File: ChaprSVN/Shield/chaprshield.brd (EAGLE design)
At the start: 100 x 80 mm, 2 parts

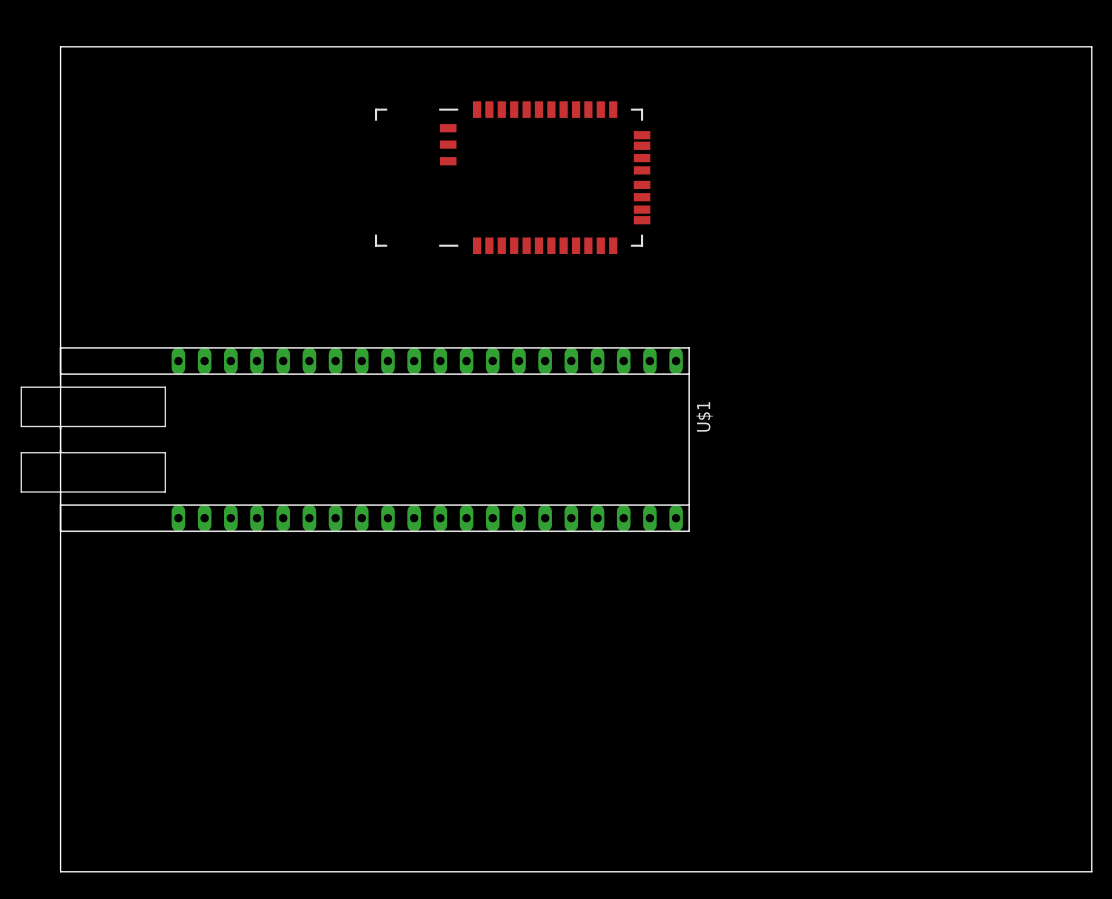
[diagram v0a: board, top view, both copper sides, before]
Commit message: Added pin headers and started wiring.
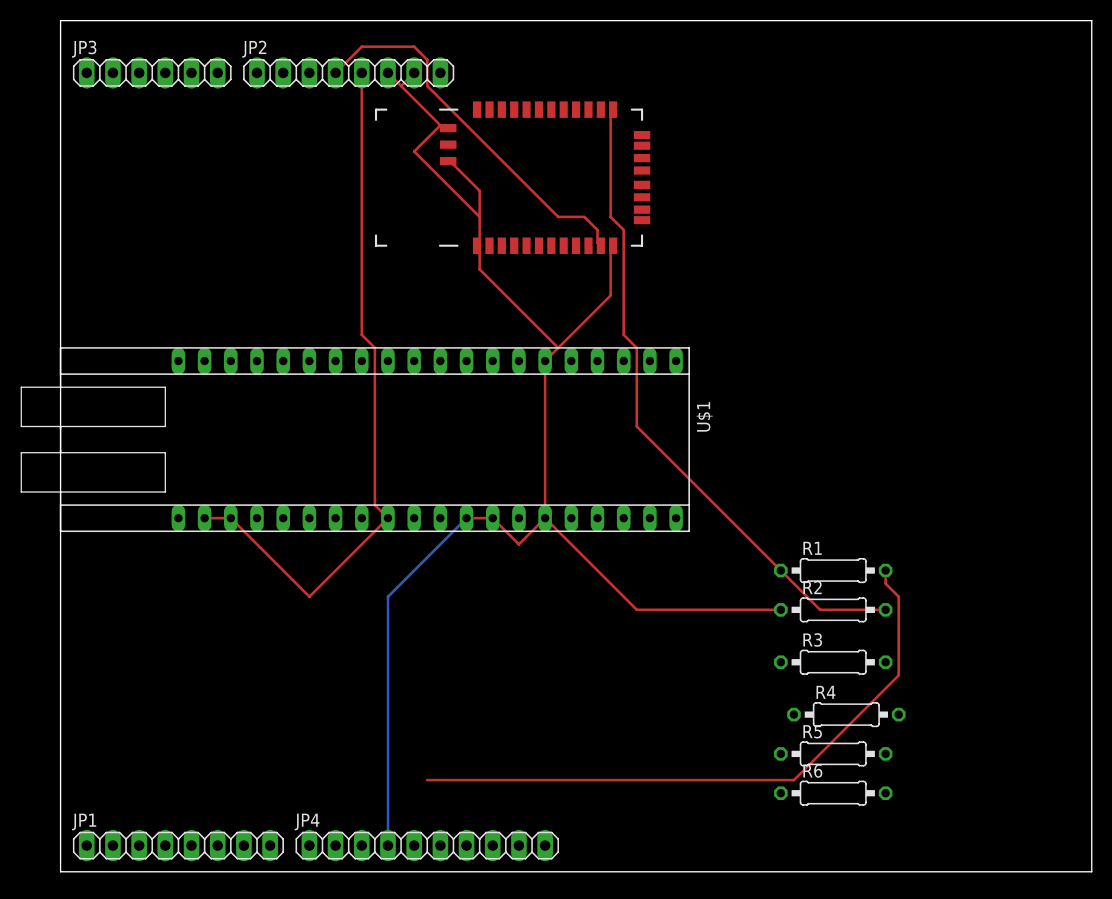
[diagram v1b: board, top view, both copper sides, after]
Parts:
- added JP1, JP2: (no value), pinhead:1X08
- added JP3: (no value), pinhead:1X06
- added JP4: (no value), pinhead:1X10
- added R1: 10k, resistor:0207/10
- added R2: 20k, resistor:0207/10
- added R3, R4, R5, R6: (no value), resistor:0207/10
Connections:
- removed net 5.0V(1): U$1.2
- removed net 5.0V(2): U$1.3
- removed net 5.0V(3): U$1.9
- new net N$1: JP2.5, U$1.2, U$1.3, U$1.9
- new net N$2: JP2.4, U$2.11
- new net N$3: JP4.5, R1.2
- new net N$4: R1.1, R2.2, U$2.13
- new net N$5: JP4.6, U$2.14
- net GND: now also JP2.6, JP2.7, JP4.4, R2.1
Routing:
- net GND: track 0.00 -> 146.1 mm
- net N$1: track 0.00 -> 68.3 mm
- net N$4: track 0.00 -> 63.4 mm
- net N$3: track 0.00 -> 60.6 mm
- net N$2: track 0.00 -> 37.0 mm
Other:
- board size 100 x 80 mm -> 100 x 82.5 mm
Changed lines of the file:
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@@
 <plain>
 <wire x1="0" y1="0" x2="100" y2="0" width="0" layer="20"/>
-<wire x1="100" y1="0" x2="100" y2="80" width="0" layer="20"/>
-<wire x1="100" y1="80" x2="0" y2="80" width="0" layer="20"/>
-<wire x1="0" y1="80" x2="0" y2="0" width="0" layer="20"/>
+<wire x1="100" y1="0" x2="100" y2="82.54" width="0" layer="20"/>
+<wire x1="100" y1="82.54" x2="0" y2="82.54" width="0" layer="20"/>
+<wire x1="0" y1="82.54" x2="0" y2="0" width="0" layer="20"/>
 </plain>
 <attributes>
@@
 <param name="RoutingGrid" value="50mil"/>
 <param name="tpViaShape" value="round"/>
-<param name="PrefDir.1" value="|"/>
+<param name="PrefDir.1" value="\"/>
 <param name="PrefDir.2" value="0"/>
 <param name="PrefDir.3" value="0"/>
@@
 <param name="PrefDir.14" value="0"/>
 <param name="PrefDir.15" value="0"/>
-<param name="PrefDir.16" value="-"/>
+<param name="PrefDir.16" value="*"/>
 <param name="cfVia" value="8"/>
 <param name="cfNonPref" value="5"/>
@@
 <element name="U$1" library="ChapR-Custom" package="VDIP2" value="VDIP2" x="35.56" y="41.91"/>
 <element name="U$2" library="SparkFun-RF" package="RN41" value="BLUETOOTH-RN41&quot;" x="46.99" y="67.31"/>
+<element name="JP1" library="pinhead" package="1X08" value="" x="11.43" y="2.54"/>
+<element name="JP2" library="pinhead" package="1X08" value="" x="27.94" y="77.47"/>
+<element name="JP3" library="pinhead" package="1X06" value="" x="8.89" y="77.47"/>
+<element name="JP4" library="pinhead" package="1X10" value="" x="35.56" y="2.54"/>
+<element name="R1" library="resistor" package="0207/10" value="10k" x="74.93" y="29.21"/>
+<element name="R2" library="resistor" package="0207/10" value="20k" x="74.93" y="25.4"/>
+<element name="R3" library="resistor" package="0207/10" value="" x="74.93" y="20.32"/>
+<element name="R4" library="resistor" package="0207/10" value="" x="76.2" y="15.24"/>
+<element name="R5" library="resistor" package="0207/10" value="" x="74.93" y="11.43"/>
+<element name="R6" library="resistor" package="0207/10" value="" x="74.93" y="7.62"/>
 </elements>
 <signals>
 <signal name="3.3V(2)">
 <contactref element="U$1" pad="38"/>
-</signal>
-<signal name="5.0V(1)">
-<contactref element="U$1" pad="2"/>
-</signal>
-<signal name="5.0V(2)">
-<contactref element="U$1" pad="3"/>
-</signal>
-<signal name="5.0V(3)">
-<contactref element="U$1" pad="9"/>
 </signal>
 <signal name="NC(1)">
@@
 <contactref element="U$2" pad="28"/>
 <contactref element="U$2" pad="29"/>
+<contactref element="JP4" pad="4"/>
+<contactref element="JP2" pad="6"/>
+<contactref element="JP2" pad="7"/>
+<contactref element="R2" pad="1"/>
+<wire x1="31.75" y1="77.47" x2="33.02" y2="76.2" width="0.254" layer="1"/>
+<wire x1="33.02" y1="76.2" x2="36.83" y2="72.39" width="0.254" layer="1"/>
+<wire x1="33.02" y1="76.2" x2="34.29" y2="77.47" width="0.254" layer="1"/>
+<wire x1="40.64" y1="66.04" x2="40.64" y2="63.5" width="0.254" layer="1"/>
+<wire x1="40.64" y1="63.5" x2="40.64" y2="60.96" width="0.254" layer="1"/>
+<wire x1="38.1" y1="68.58" x2="40.64" y2="66.04" width="0.254" layer="1"/>
+<wire x1="38.1" y1="68.58" x2="37.59" y2="68.91" width="0.254" layer="1"/>
+<wire x1="53.34" y1="55.88" x2="53.34" y2="60.96" width="0.254" layer="1"/>
+<wire x1="46.99" y1="49.53" x2="48.26" y2="50.8" width="0.254" layer="1"/>
+<wire x1="48.26" y1="50.8" x2="53.34" y2="55.88" width="0.254" layer="1"/>
+<wire x1="53.34" y1="60.96" x2="53.59" y2="60.71" width="0.254" layer="1"/>
+<wire x1="40.64" y1="58.42" x2="40.64" y2="60.96" width="0.254" layer="1"/>
+<wire x1="48.26" y1="50.8" x2="40.64" y2="58.42" width="0.254" layer="1"/>
+<wire x1="40.64" y1="60.96" x2="40.39" y2="60.71" width="0.254" layer="1"/>
+<wire x1="34.29" y1="69.85" x2="36.83" y2="72.39" width="0.254" layer="1"/>
+<wire x1="40.64" y1="63.5" x2="34.29" y2="69.85" width="0.254" layer="1"/>
+<wire x1="36.83" y1="72.39" x2="37.59" y2="72.11" width="0.254" layer="1"/>
+<wire x1="41.91" y1="34.29" x2="39.37" y2="34.29" width="0.254" layer="1"/>
+<wire x1="44.45" y1="31.75" x2="46.99" y2="34.29" width="0.254" layer="1"/>
+<wire x1="41.91" y1="34.29" x2="44.45" y2="31.75" width="0.254" layer="1"/>
+<wire x1="55.88" y1="25.4" x2="69.85" y2="25.4" width="0.254" layer="1"/>
+<wire x1="46.99" y1="34.29" x2="55.88" y2="25.4" width="0.254" layer="1"/>
+<wire x1="31.75" y1="26.67" x2="31.75" y2="2.54" width="0.254" layer="16"/>
+<wire x1="39.37" y1="34.29" x2="31.75" y2="26.67" width="0.254" layer="16"/>
+<wire x1="46.99" y1="34.29" x2="46.99" y2="49.53" width="0.254" layer="1"/>
 <wire x1="56.39" y1="64.21" x2="56.39" y2="70.41" width="0" layer="19" extent="1-1"/>
-<wire x1="53.59" y1="60.71" x2="56.39" y2="64.21" width="0" layer="19" extent="1-1"/>
-<wire x1="46.99" y1="49.53" x2="53.59" y2="60.71" width="0" layer="19" extent="1-1"/>
-<wire x1="40.39" y1="60.71" x2="46.99" y2="49.53" width="0" layer="19" extent="1-1"/>
-<wire x1="37.59" y1="68.91" x2="40.39" y2="60.71" width="0" layer="19" extent="1-1"/>
-<wire x1="37.59" y1="72.11" x2="37.59" y2="68.91" width="0" layer="19" extent="1-1"/>
-<wire x1="46.99" y1="34.29" x2="46.99" y2="49.53" width="0" layer="19" extent="1-1"/>
-<wire x1="41.91" y1="34.29" x2="46.99" y2="34.29" width="0" layer="19" extent="1-1"/>
-<wire x1="39.37" y1="34.29" x2="41.91" y2="34.29" width="0" layer="19" extent="1-1"/>
+<wire x1="53.34" y1="60.96" x2="56.39" y2="64.21" width="0" layer="19" extent="1-1"/>
+</signal>
+<signal name="N$1">
+<contactref element="JP2" pad="5"/>
+<contactref element="U$1" pad="9"/>
+<contactref element="U$1" pad="3"/>
+<contactref element="U$1" pad="2"/>
+<wire x1="16.51" y1="34.29" x2="13.97" y2="34.29" width="0.254" layer="1"/>
+<wire x1="24.13" y1="26.67" x2="31.75" y2="34.29" width="0.254" layer="1"/>
+<wire x1="16.51" y1="34.29" x2="24.13" y2="26.67" width="0.254" layer="1"/>
+<wire x1="29.21" y1="52.07" x2="29.21" y2="77.47" width="0.254" layer="1"/>
+<wire x1="30.48" y1="50.8" x2="29.21" y2="52.07" width="0.254" layer="1"/>
+<wire x1="30.48" y1="35.56" x2="30.48" y2="50.8" width="0.254" layer="1"/>
+<wire x1="31.75" y1="34.29" x2="30.48" y2="35.56" width="0.254" layer="1"/>
+</signal>
+<signal name="N$2">
+<contactref element="JP2" pad="4"/>
+<contactref element="U$2" pad="11"/>
+<wire x1="52.07" y1="62.23" x2="52.07" y2="60.96" width="0.254" layer="1"/>
+<wire x1="50.8" y1="63.5" x2="52.07" y2="62.23" width="0.254" layer="1"/>
+<wire x1="48.26" y1="63.5" x2="50.8" y2="63.5" width="0.254" layer="1"/>
+<wire x1="35.56" y1="76.2" x2="48.26" y2="63.5" width="0.254" layer="1"/>
+<wire x1="35.56" y1="78.74" x2="35.56" y2="76.2" width="0.254" layer="1"/>
+<wire x1="34.29" y1="80.01" x2="35.56" y2="78.74" width="0.254" layer="1"/>
+<wire x1="29.21" y1="80.01" x2="34.29" y2="80.01" width="0.254" layer="1"/>
+<wire x1="26.67" y1="77.47" x2="29.21" y2="80.01" width="0.254" layer="1"/>
+<wire x1="52.07" y1="60.96" x2="52.39" y2="60.71" width="0.254" layer="1"/>
+</signal>
+<signal name="N$3">
+<contactref element="R1" pad="2"/>
+<wire x1="80.01" y1="27.94" x2="80.01" y2="29.21" width="0.254" layer="1"/>
+<wire x1="81.28" y1="26.67" x2="80.01" y2="27.94" width="0.254" layer="1"/>
+<wire x1="81.28" y1="19.05" x2="81.28" y2="26.67" width="0.254" layer="1"/>
+<wire x1="71.12" y1="8.89" x2="81.28" y2="19.05" width="0.254" layer="1"/>
+<wire x1="35.56" y1="8.89" x2="71.12" y2="8.89" width="0.254" layer="1"/>
+<contactref element="JP4" pad="5"/>
+<wire x1="34.29" y1="2.54" x2="35.56" y2="8.89" width="0" layer="19" extent="1-1"/>
+</signal>
+<signal name="N$4">
+<contactref element="R1" pad="1"/>
+<contactref element="R2" pad="2"/>
+<contactref element="U$2" pad="13"/>
+<wire x1="53.34" y1="63.5" x2="53.34" y2="73.66" width="0.254" layer="1"/>
+<wire x1="54.61" y1="62.23" x2="53.34" y2="63.5" width="0.254" layer="1"/>
+<wire x1="54.61" y1="52.07" x2="54.61" y2="62.23" width="0.254" layer="1"/>
+<wire x1="55.88" y1="50.8" x2="54.61" y2="52.07" width="0.254" layer="1"/>
+<wire x1="55.88" y1="43.18" x2="55.88" y2="50.8" width="0.254" layer="1"/>
+<wire x1="69.85" y1="29.21" x2="55.88" y2="43.18" width="0.254" layer="1"/>
+<wire x1="53.34" y1="73.66" x2="53.59" y2="73.91" width="0.254" layer="1"/>
+<wire x1="73.66" y1="25.4" x2="80.01" y2="25.4" width="0.254" layer="1"/>
+<wire x1="69.85" y1="29.21" x2="73.66" y2="25.4" width="0.254" layer="1"/>
+</signal>
+<signal name="N$5">
+<contactref element="U$2" pad="14"/>
+<contactref element="JP4" pad="6"/>
+<wire x1="36.83" y1="2.54" x2="52.39" y2="73.91" width="0" layer="19" extent="1-1"/>
 </signal>
 </signals>

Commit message: 
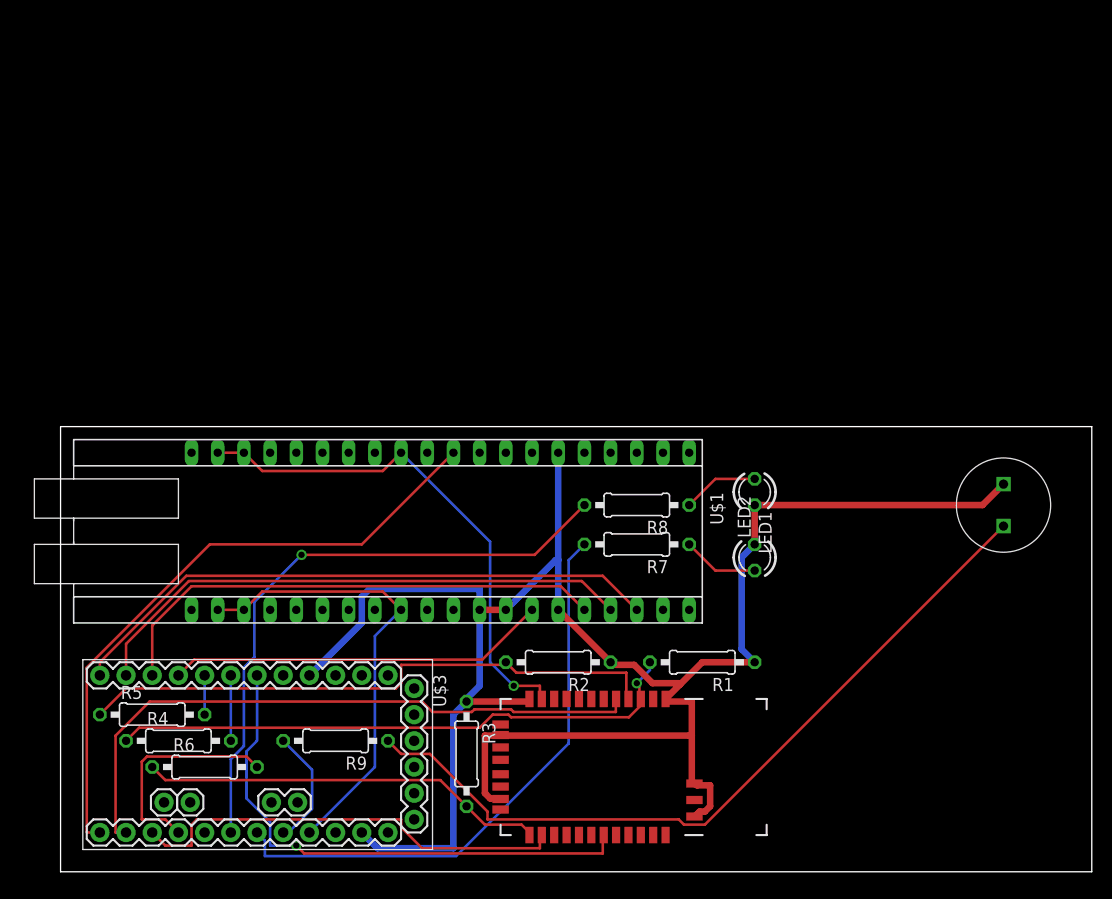
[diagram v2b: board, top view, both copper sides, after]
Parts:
- removed JP1, JP2: (no value), pinhead:1X08
- removed JP3: (no value), pinhead:1X06
- removed JP4: (no value), pinhead:1X10
- added LED1, LED2: (no value), led:LED3MM
- added M2: RN42 Module, SparkFun-RF:RN41
- added R7, R8: 470, resistor:0207/10
- added R9: 100, resistor:0207/10
- added U$3: PROMINI, ChapR-Custom:PROMINI
- R1: value 10k -> 20k
- R3: value (none) -> 20k
- R4, R5, R6: value (none) -> 10k
- U$2: value BLUETOOTH-RN41" -> SPEAKER; device SparkFun-RF:RN41 -> ChapR-Custom:SPEAKER
- moved R5 66.1 mm to (8.89, 15.2)
- moved R4 64.8 mm to (11.4, 12.7)
- moved R6 61.0 mm to (14.0, 10.2)
- moved U$2 54.6 mm to (91.4, 35.6), turned to 90 degrees
- moved R3 36.7 mm to (39.4, 11.4), turned to 270 degrees
- moved R2 27.1 mm to (48.3, 20.3), turned to 180 degrees
- moved R1 15.5 mm to (62.2, 20.3), turned to 180 degrees
- moved U$1 8.98 mm to (36.8, 33.0)
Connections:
- removed net 3.3V(2): U$1.38
- new net +9V: U$3.RAWV
- new net 3.3V: M2.11, U$1.32, U$1.38, U$1.39
- new net N$10: U$1.18, U$3.D9
- new net N$11: U$1.17, U$3.D8
- new net N$12: U$1.16, U$3.D7
- new net N$13: U$1.14, U$3.D6
- new net N$14: R4.2, U$3.D4
- new net N$15: M2.19, U$3.D3
- new net N$16: LED2.A, R7.1
- new net N$17: LED1.A, R8.1
- new net N$18: R7.2, U$3.A2
- new net N$19: R9.1, U$2.+
- new net N$20: R8.2, U$3.A1
- new net N$21: R9.2, U$3.A3
- new net N$6: M2.3, R1.2, R4.1
- new net N$7: M2.4, R2.2, R5.1
- new net N$8: R5.2, U$3.D5
- new net N$9: M2.13, R3.2, R6.1
- net GND: now also LED1.K, LED2.K, M2.1, M2.12, M2.25, M2.27, M2.28, M2.29, R1.1, R3.1, U$2.-, U$3.GND, U$3.GND2; no longer JP2.6, JP2.7, JP4.4, U$2.1, U$2.12, U$2.25, U$2.27, U$2.28, U$2.29
- net N$1: now also U$3.VCC; no longer JP2.5
- net N$2: now also U$1.30, U$3.D10; no longer JP2.4, U$2.11
- net N$3: now also R6.2, U$3.D13; no longer JP4.5, R1.2
- net N$4: now also M2.14, U$3.D12; no longer R1.1, R2.2, U$2.13
- net N$5: now also M2.5, U$3.D11; no longer JP4.6, U$2.14
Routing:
- net N$19: track 0.00 -> 75.5 mm
- net N$5: track 0.00 -> 62.2 mm
- net N$20: track 0.00 -> 59.2 mm, vias 0 -> 1
- net N$10: track 0.00 -> 58.2 mm
- net N$7: track 0.00 -> 57.9 mm
- net N$6: track 0.00 -> 56.6 mm, vias 0 -> 1
- net N$18: track 0.00 -> 56.5 mm
- net N$11: track 0.00 -> 53.7 mm
- net N$15: track 0.00 -> 52.3 mm, vias 0 -> 1
- net GND: track 146.1 -> 198.5 mm
- net 3.3V: track 0.00 -> 50.4 mm, vias 0 -> 1
- net N$12: track 0.00 -> 49.3 mm
- net N$9: track 0.00 -> 39.5 mm
- net N$3: track 60.6 -> 21.5 mm
- net N$13: track 0.00 -> 36.9 mm
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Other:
- board size 100 x 82.5 mm -> 100 x 43.2 mm

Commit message: added power connector, placed holes
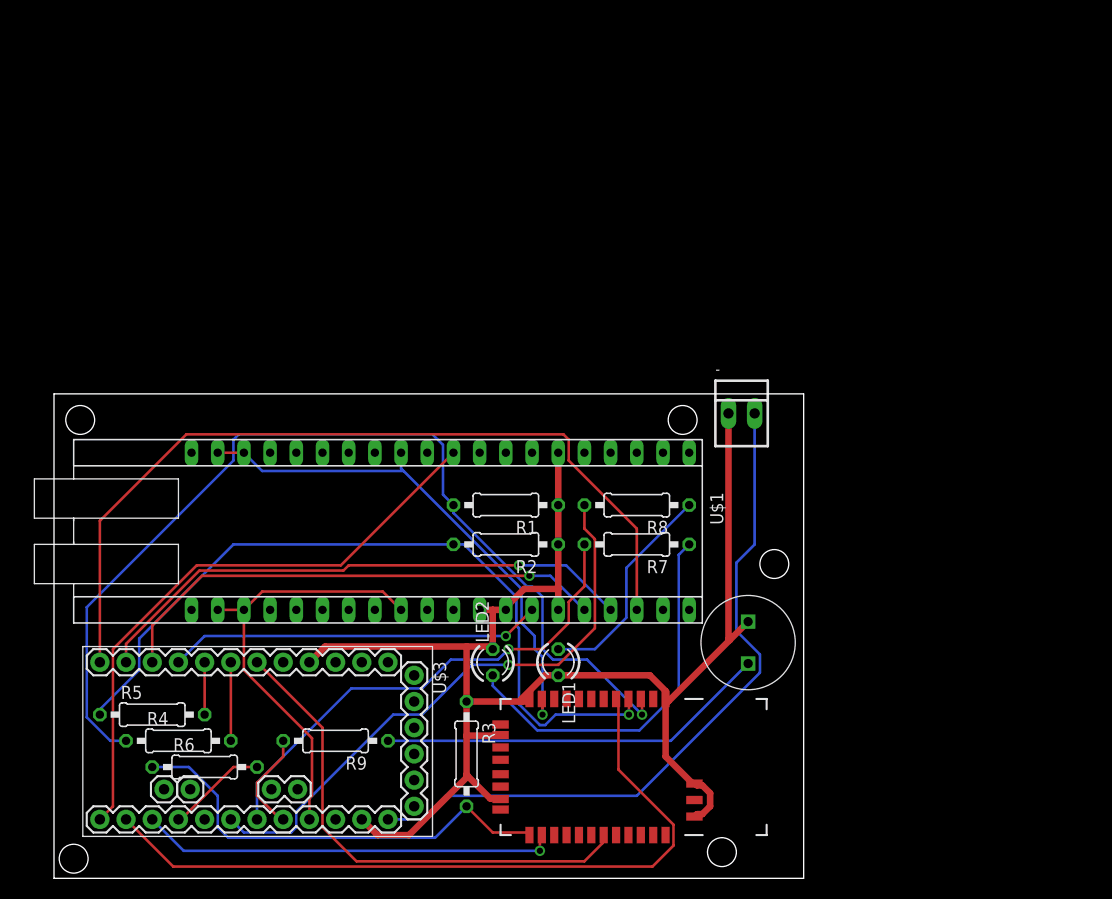
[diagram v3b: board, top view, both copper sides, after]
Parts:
- added -: 9v power, con-molex:22-23-2021
- moved U$2 28.1 mm to (66.7, 22.2)
- moved LED2 27.4 mm to (41.9, 20.3)
- moved LED1 25.2 mm to (48.3, 20.3)
- moved R1 24.4 mm to (43.2, 35.6)
- moved R2 12.5 mm to (43.2, 31.8)
- moved U$3 1.27 mm to (19.1, 11.4)
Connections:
- net +9V: now also -.2
- net GND: now also -.1
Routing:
- net +9V: track 0.00 -> 68.8 mm
- net GND: track 198.5 -> 150.3 mm
- net N$6: track 56.6 -> 96.5 mm
- net N$19: track 75.5 -> 38.0 mm
- net N$16: track 7.40 -> 37.1 mm
- net N$10: track 58.2 -> 82.1 mm
- net N$7: track 57.9 -> 75.4 mm, vias 0 -> 1
- net N$17: track 7.40 -> 21.3 mm
- net N$3: track 21.5 -> 9.72 mm
- net N$5: track 62.2 -> 72.3 mm
- net N$18: track 56.5 -> 48.5 mm, vias 0 -> 1
- net N$9: track 39.5 -> 43.8 mm
- net N$15: track 52.3 -> 48.8 mm, vias 1 -> 0
- net N$2: track 61.5 -> 57.9 mm
- net N$4: track 43.4 -> 40.6 mm, vias 0 -> 1
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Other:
- board size 100 x 43.2 mm -> 72.7 x 47 mm
